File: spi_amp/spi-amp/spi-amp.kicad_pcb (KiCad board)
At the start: 4 copper layers, 28.7 x 64.4 mm, 27 parts, among them J1 IN+, J2 IN-, J3 OUT+, J4 OUT-, J5 Conn_01x06, U1 LMH6401, U2 LM78M05_TO220

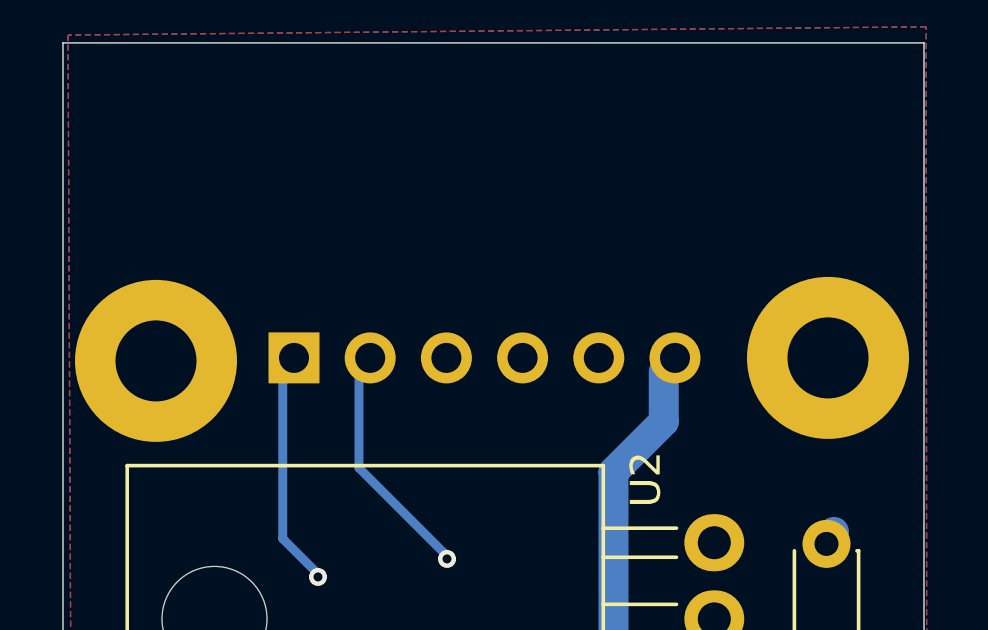
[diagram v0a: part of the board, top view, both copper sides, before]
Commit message: Finalized SPI interface PCB
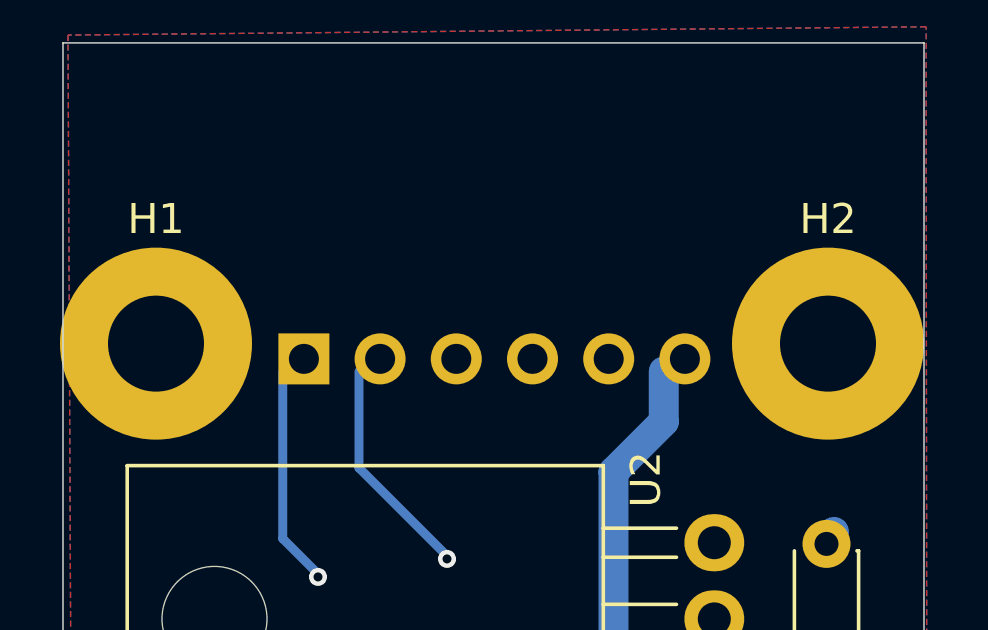
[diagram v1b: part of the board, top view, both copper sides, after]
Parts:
- H1, H2: footprint MountingHole:MountingHole_2.7mm_M2.5_Pad -> MountingHole:MountingHole_3.2mm_M3_Pad
- moved H1 0.58 mm to (108.1, 52.3)
- moved H2 0.48 mm to (130.5, 52.3)
- moved J5 0.33 mm to (113.0, 52.8)
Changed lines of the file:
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@@
 		)
 	)
-	(footprint "MountingHole:MountingHole_2.7mm_M2.5_Pad"
+	(footprint "MountingHole:MountingHole_3.2mm_M3_Pad"
 		(layer "F.Cu")
-		(at 108.1 52.9)
-		(descr "Mounting Hole 2.7mm, M2.5, generated by kicad-footprint-generator mountinghole.py")
-		(tags "mountinghole M2.5")
+		(at 108.1 52.324)
+		(descr "Mounting Hole 3.2mm, M3, generated by kicad-footprint-generator mountinghole.py")
+		(tags "mountinghole M3")
 		(property "Reference" "H1"
-			(at 0 -3.65 0)
+			(at 0 -4.15 0)
 			(layer "F.SilkS")
-			(hide yes)
 			(effects
 				(font
@@
 		)
 		(property "Value" "MountingHole_Pad"
-			(at 0 3.65 0)
+			(at 0 4.15 0)
 			(layer "F.Fab")
 			(effects
@@
 		(fp_circle
 			(center 0 0)
-			(end 2.7 0)
+			(end 3.2 0)
 			(stroke
 				(width 0.15)
@@
 		(fp_circle
 			(center 0 0)
-			(end 2.95 0)
+			(end 3.45 0)
 			(stroke
 				(width 0.05)
@@
 		(pad "1" thru_hole circle
 			(at 0 0)
-			(size 5.4 5.4)
-			(drill 2.7)
+			(size 6.4 6.4)
+			(drill 3.2)
 			(layers "*.Cu" "*.Mask")
 			(remove_unused_layers no)
@@
 		)
 	)
-	(footprint "MountingHole:MountingHole_2.7mm_M2.5_Pad"
+	(footprint "MountingHole:MountingHole_3.2mm_M3_Pad"
 		(layer "F.Cu")
-		(at 130.5 52.8)
-		(descr "Mounting Hole 2.7mm, M2.5, generated by kicad-footprint-generator mountinghole.py")
-		(tags "mountinghole M2.5")
+		(at 130.5 52.324)
+		(descr "Mounting Hole 3.2mm, M3, generated by kicad-footprint-generator mountinghole.py")
+		(tags "mountinghole M3")
 		(property "Reference" "H2"
-			(at 0 -3.65 0)
+			(at 0 -4.15 0)
 			(layer "F.SilkS")
-			(hide yes)
 			(effects
 				(font
@@
 		)
 		(property "Value" "MountingHole_Pad"
-			(at 0 3.65 0)
+			(at 0 4.15 0)
 			(layer "F.Fab")
 			(effects
@@
 		(fp_circle
 			(center 0 0)
-			(end 2.7 0)
+			(end 3.2 0)
 			(stroke
 				(width 0.15)
@@
 		(fp_circle
 			(center 0 0)
-			(end 2.95 0)
+			(end 3.45 0)
 			(stroke
 				(width 0.05)
@@
 		(pad "1" thru_hole circle
 			(at 0 0)
-			(size 5.4 5.4)
-			(drill 2.7)
+			(size 6.4 6.4)
+			(drill 3.2)
 			(layers "*.Cu" "*.Mask")
 			(remove_unused_layers no)
@@
 	(footprint "Connector_PinSocket_2.54mm:PinSocket_1x06_P2.54mm_Horizontal"
 		(layer "B.Cu")
-		(at 112.7 52.8 -90)
+		(at 113.03 52.832 -90)
 		(descr "Through hole angled socket strip, 1x06, 2.54mm pitch, 8.51mm socket length, single row (from Kicad 4.0.7), script generated")
 		(tags "Through hole angled socket strip THT 1x06 2.54mm single row")
 		(property "Reference" "J5"
-			(at -2.5 2.3 90)
+			(at -7.62 3.302 90)
 			(layer "B.SilkS")
 			(effects

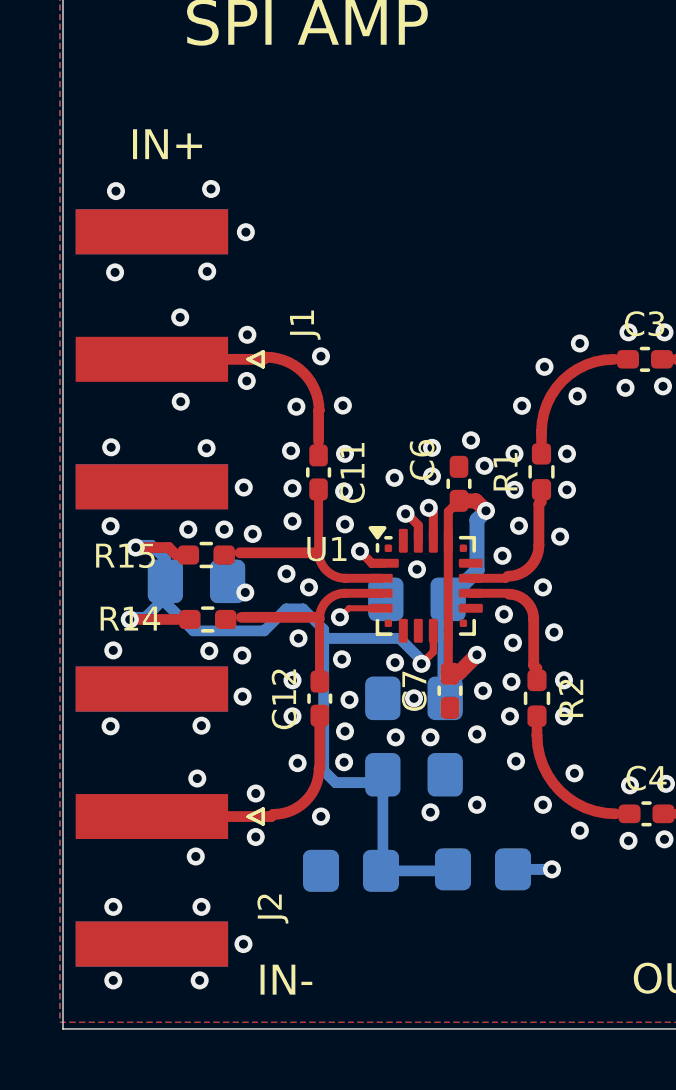
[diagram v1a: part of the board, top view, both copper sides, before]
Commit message: Fixed balun connector distance.
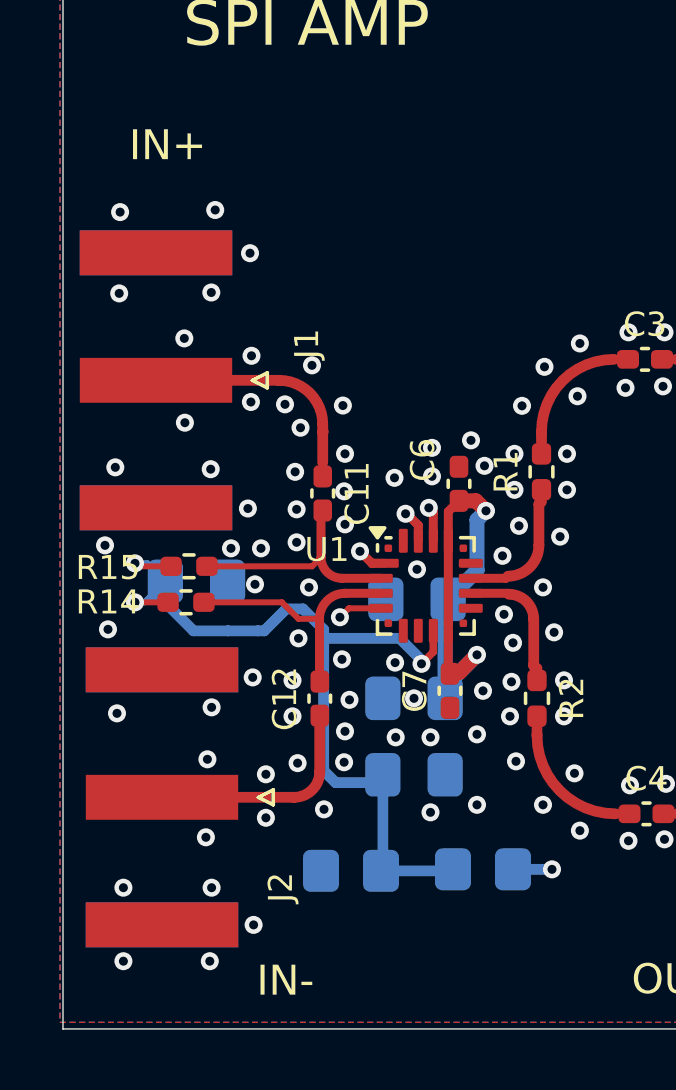
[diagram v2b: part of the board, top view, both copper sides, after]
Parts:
- moved R14 0.92 mm to (109.1, 92.5)
- moved J2 0.72 mm to (108.3, 99.0)
- moved C11 0.71 mm to (113.7, 88.9)
- moved J1 0.71 mm to (108.1, 85.1)
- moved R15 0.69 mm to (109.2, 91.3)
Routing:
- net Net-(U1-Vocm): track 31.9 -> 30.3 mm
- net Net-(C12-Pad2): track 7.22 -> 8.67 mm
- net Net-(C11-Pad2): track 7.33 -> 7.95 mm
- net Net-(J2-In): track 8.19 -> 7.58 mm
- net DIG_GND: vias 130 -> 127

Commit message: Finalized the PCBs and sent them to review.
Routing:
- net DIG_GND: vias 127 -> 141
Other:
- board size 28.7 x 64.4 mm -> 28.7 x 66.1 mm
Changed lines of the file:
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@@
 	)
 	(gr_rect
-		(start 105 42.3)
+		(start 105 40.6)
 		(end 133.7 106.72)
 		(stroke
@@
 	)
 	(via
+		(at 115.7 43.55)
+		(size 0.6)
+		(drill 0.3)
+		(layers "F.Cu" "B.Cu")
+		(free yes)
+		(net "DIG_GND")
+	)
+	(via
 		(at 125 85.3)
 		(size 0.6)
@@
 	)
 	(via
+		(at 106.05 67.85)
+		(size 0.6)
+		(drill 0.3)
+		(layers "F.Cu" "B.Cu")
+		(free yes)
+		(net "DIG_GND")
+	)
+	(via
 		(at 113.7 99.4)
 		(size 0.6)
@@
 	)
 	(via
+		(at 132.65 56.1)
+		(size 0.6)
+		(drill 0.3)
+		(layers "F.Cu" "B.Cu")
+		(free yes)
+		(net "DIG_GND")
+	)
+	(via
 		(at 111.6 90.7)
 		(size 0.6)
@@
 	)
 	(via
+		(at 106.15 48)
+		(size 0.6)
+		(drill 0.3)
+		(layers "F.Cu" "B.Cu")
+		(free yes)
+		(net "DIG_GND")
+	)
+	(via
+		(at 122.2 43.45)
+		(size 0.6)
+		(drill 0.3)
+		(layers "F.Cu" "B.Cu")
+		(free yes)
+		(net "DIG_GND")
+	)
+	(via
 		(at 112.85 93.7)
 		(size 0.6)
@@
 	)
 	(via
+		(at 132.4 47.85)
+		(size 0.6)
+		(drill 0.3)
+		(layers "F.Cu" "B.Cu")
+		(free yes)
+		(net "DIG_GND")
+	)
+	(via
 		(at 109.8935 104.462)
 		(size 0.6)
@@
 	)
 	(via
+		(at 123.25 68.9)
+		(size 0.6)
+		(drill 0.3)
+		(layers "F.Cu" "B.Cu")
+		(free yes)
+		(net "DIG_GND")
+	)
+	(via
 		(at 132.23 89.87)
 		(size 0.6)
@@
 	)
 	(via
+		(at 132.55 61.35)
+		(size 0.6)
+		(drill 0.3)
+		(layers "F.Cu" "B.Cu")
+		(free yes)
+		(net "DIG_GND")
+	)
+	(via
 		(at 127.81 80.1)
 		(size 0.6)
@@
 	)
 	(via
+		(at 132.55 70.9)
+		(size 0.6)
+		(drill 0.3)
+		(layers "F.Cu" "B.Cu")
+		(free yes)
+		(net "DIG_GND")
+	)
+	(via
 		(at 107.0135 104.462)
 		(size 0.6)
@@
 	)
 	(via
+		(at 132.4 43.45)
+		(size 0.6)
+		(drill 0.3)
+		(layers "F.Cu" "B.Cu")
+		(free yes)
+		(net "DIG_GND")
+	)
+	(via
+		(at 106.05 56.65)
+		(size 0.6)
+		(drill 0.3)
+		(layers "F.Cu" "B.Cu")
+		(free yes)
+		(net "DIG_GND")
+	)
+	(via
 		(at 121.57 90.31)
 		(size 0.6)
@@
 	)
 	(via
+		(at 106.3 62.5)
+		(size 0.6)
+		(drill 0.3)
+		(layers "F.Cu" "B.Cu")
+		(free yes)
+		(net "DIG_GND")
+	)
+	(via
 		(at 127.29 85.15)
 		(size 0.6)
@@
 	)
 	(via
+		(at 106.3 43.4)
+		(size 0.6)
+		(drill 0.3)
+		(layers "F.Cu" "B.Cu")
+		(free yes)
+		(net "DIG_GND")
+	)
+	(via
 		(at 120.2 89.95)
 		(size 0.6)
@@
 		(size 0.6)
 		(drill 0.3)
+		(layers "F.Cu" "B.Cu")
+		(free yes)
+		(net "DIG_GND")
+	)
+	(via
+		(at 132.4 67.25)
+		(size 0.6)
+		(drill 0.3)
